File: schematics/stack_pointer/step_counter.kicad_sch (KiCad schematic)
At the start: 16 parts, among them U1 74HC00, U2 74HC193, U3 74HC193, U4 74HC193, U5 74HC193, U6 74HC245, U7 74HC245

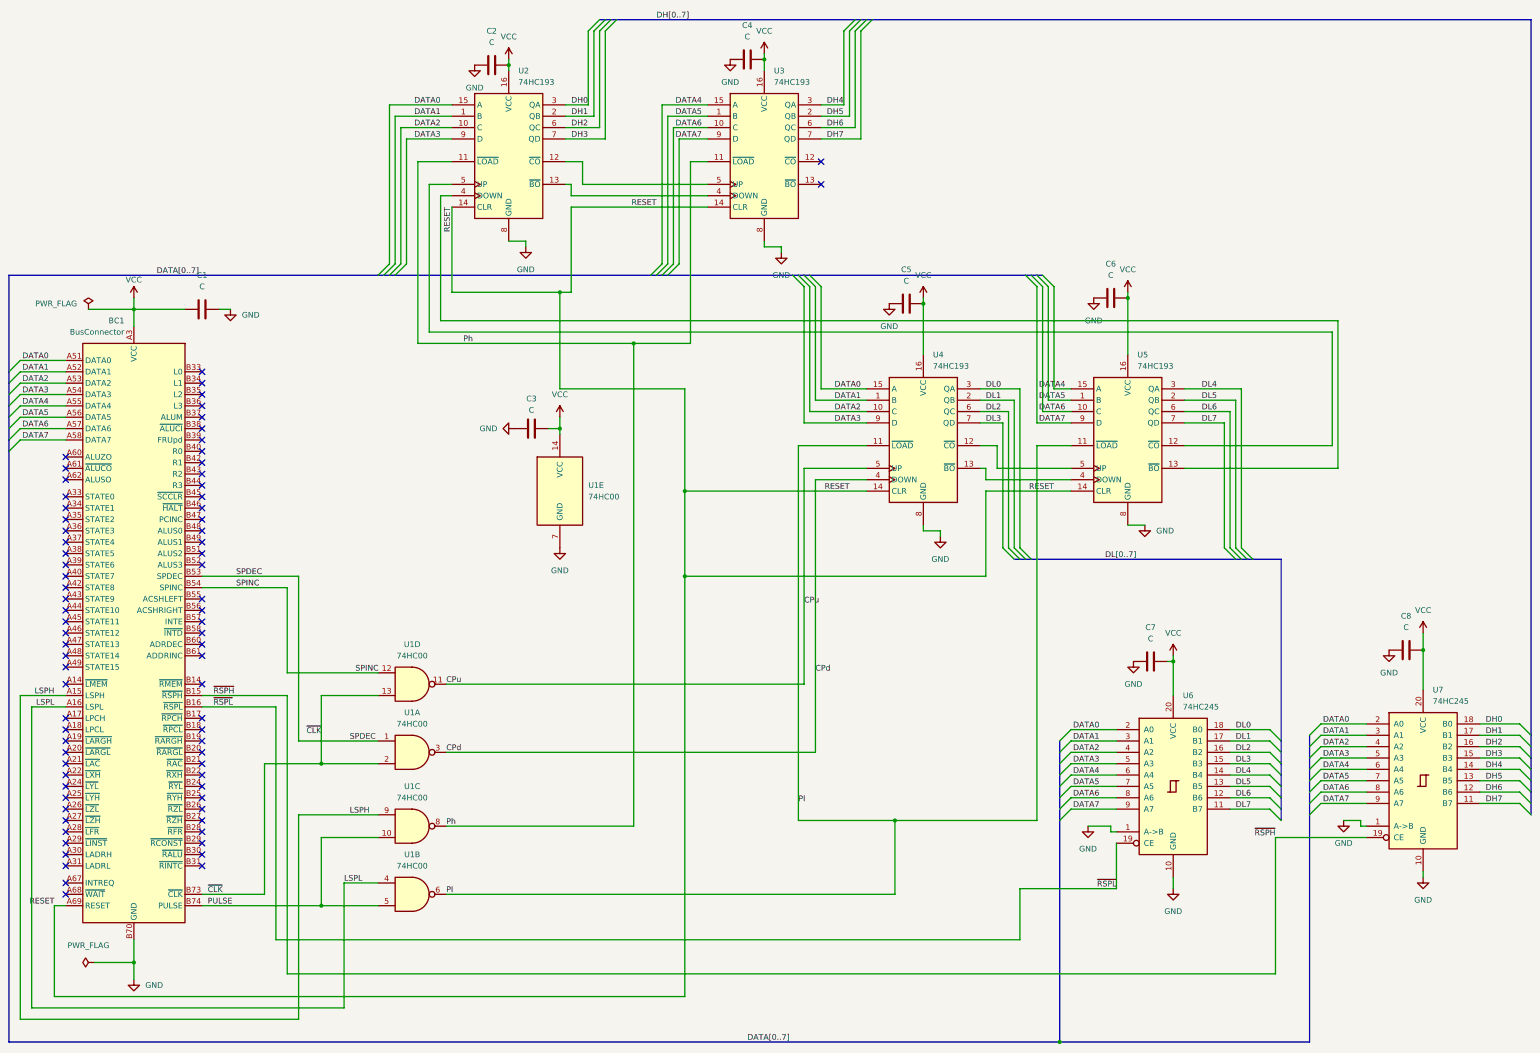
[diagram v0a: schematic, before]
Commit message: Add test points
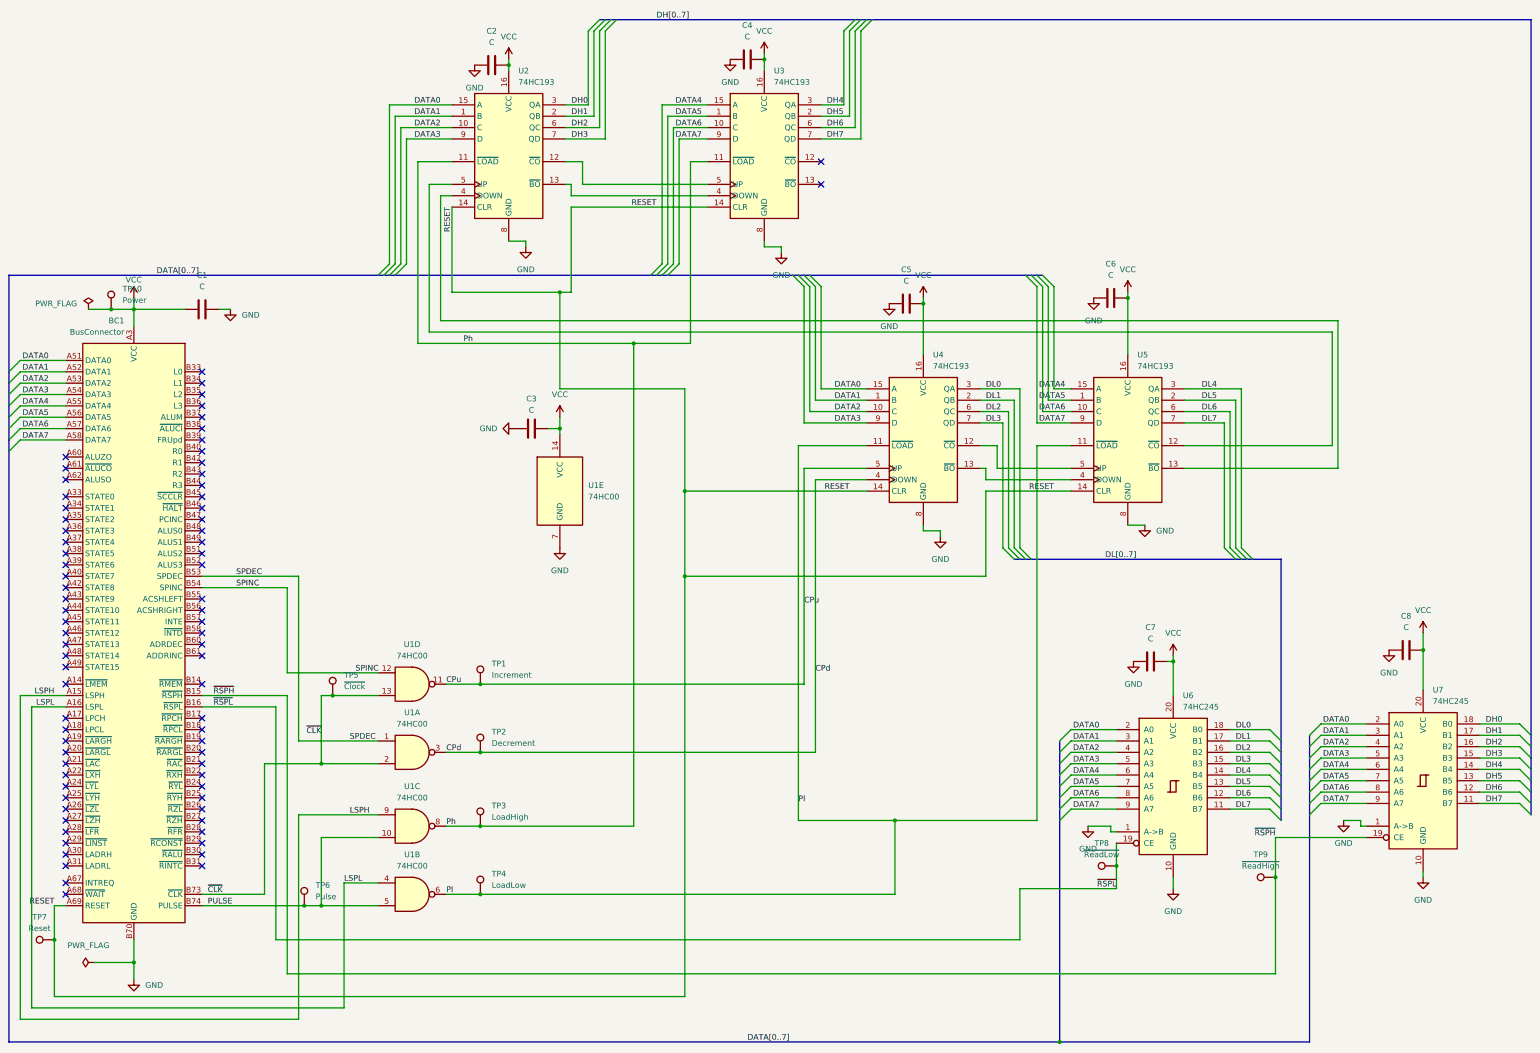
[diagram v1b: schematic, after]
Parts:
- added TP1: Increment, Connector_Pin:Pin_D1.0mm_L10.0mm, symbol Connector:TestPoint
- added TP10: Power, Connector_Pin:Pin_D1.0mm_L10.0mm, symbol Connector:TestPoint
- added TP2: Decrement, Connector_Pin:Pin_D1.0mm_L10.0mm, symbol Connector:TestPoint
- added TP3: LoadHigh, Connector_Pin:Pin_D1.0mm_L10.0mm, symbol Connector:TestPoint
- added TP4: LoadLow, Connector_Pin:Pin_D1.0mm_L10.0mm, symbol Connector:TestPoint
- added TP5: ~{Clock}, Connector_Pin:Pin_D1.0mm_L10.0mm, symbol Connector:TestPoint
- added TP6: Pulse, Connector_Pin:Pin_D1.0mm_L10.0mm, symbol Connector:TestPoint
- added TP7: Reset, Connector_Pin:Pin_D1.0mm_L10.0mm, symbol Connector:TestPoint
- added TP8: ~{ReadLow}, Connector_Pin:Pin_D1.0mm_L10.0mm, symbol Connector:TestPoint
- added TP9: ~{ReadHigh}, Connector_Pin:Pin_D1.0mm_L10.0mm, symbol Connector:TestPoint
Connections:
- net CPd: now also TP2.1
- net CPu: now also TP1.1
- net PULSE: now also TP6.1
- net Ph: now also TP3.1
- net Pl: now also TP4.1
- net RESET: now also TP7.1
- net VCC: now also TP10.1
- net ~{CLK}: now also TP5.1
- net ~{RSPH}: now also TP9.1
- net ~{RSPL}: now also TP8.1

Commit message: test points sp and pc
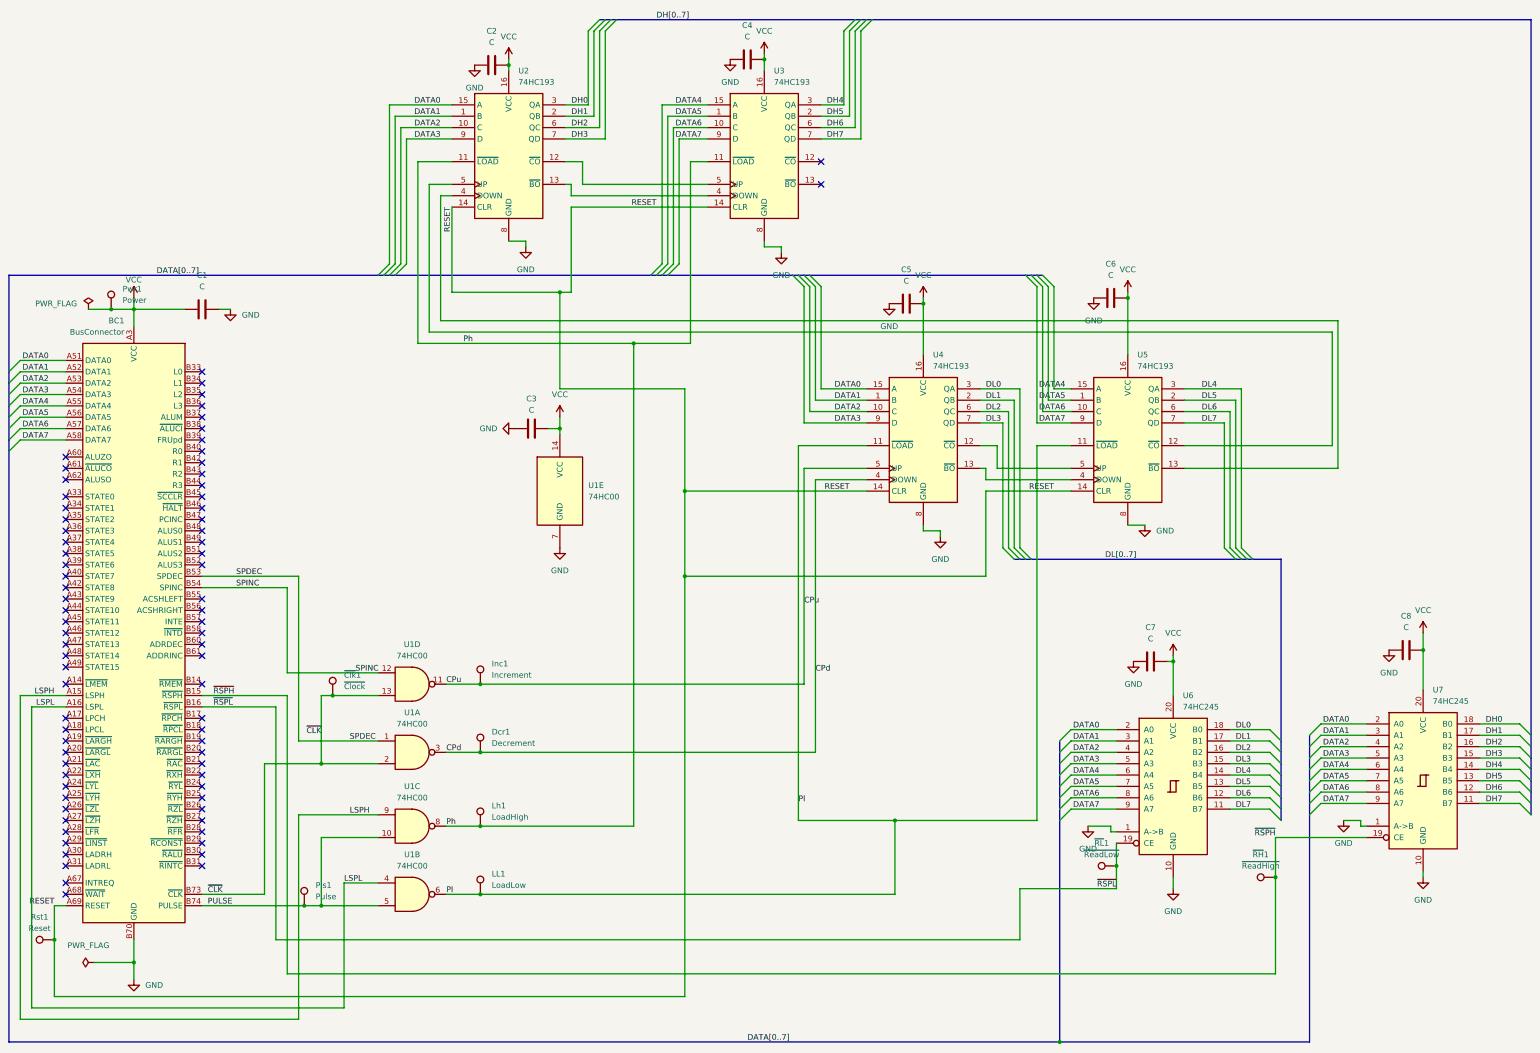
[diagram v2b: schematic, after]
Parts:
- Dcr1: renamed from TP2; footprint Connector_Pin:Pin_D1.0mm_L10.0mm -> TestPoint:TestPoint_Pad_D1.0mm
- Inc1: renamed from TP1; footprint Connector_Pin:Pin_D1.0mm_L10.0mm -> TestPoint:TestPoint_Pad_D1.0mm
- LL1: renamed from TP4; footprint Connector_Pin:Pin_D1.0mm_L10.0mm -> TestPoint:TestPoint_Pad_D1.0mm
- Lh1: renamed from TP3; footprint Connector_Pin:Pin_D1.0mm_L10.0mm -> TestPoint:TestPoint_Pad_D1.0mm
- Pls1: renamed from TP6; footprint Connector_Pin:Pin_D1.0mm_L10.0mm -> TestPoint:TestPoint_Pad_D1.0mm
- Pwr1: renamed from TP10; footprint Connector_Pin:Pin_D1.0mm_L10.0mm -> TestPoint:TestPoint_Pad_D1.0mm
- Rst1: renamed from TP7; footprint Connector_Pin:Pin_D1.0mm_L10.0mm -> TestPoint:TestPoint_Pad_D1.0mm
- ~{Clk}1: renamed from TP5; footprint Connector_Pin:Pin_D1.0mm_L10.0mm -> TestPoint:TestPoint_Pad_D1.0mm
- ~{RH}1: renamed from TP9; footprint Connector_Pin:Pin_D1.0mm_L10.0mm -> TestPoint:TestPoint_Pad_D1.0mm
- ~{RL}1: renamed from TP8; footprint Connector_Pin:Pin_D1.0mm_L10.0mm -> TestPoint:TestPoint_Pad_D1.0mm
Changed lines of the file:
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@@
 		(dnp no)
 		(fields_autoplaced yes)
-		(property "Reference" "TP6"
+		(property "Reference" "Pls1"
 			(at 101.6 215.1379 0)
 			(effects
@@
 			)
 		)
-		(property "Footprint" "Connector_Pin:Pin_D1.0mm_L10.0mm"
+		(property "Footprint" "TestPoint:TestPoint_Pad_D1.0mm"
 			(at 104.14 219.71 0)
 			(effects
@@
 			(project "step_counter"
 				(path "/f5389107-3d60-400a-ba2f-c69edfa4a2c5"
-					(reference "TP6")
+					(reference "Pls1")
 					(unit 1)
 				)
@@
 		(dnp no)
 		(fields_autoplaced yes)
-		(property "Reference" "TP3"
+		(property "Reference" "Lh1"
 			(at 140.97 197.3579 0)
 			(effects
@@
 			)
 		)
-		(property "Footprint" "Connector_Pin:Pin_D1.0mm_L10.0mm"
+		(property "Footprint" "TestPoint:TestPoint_Pad_D1.0mm"
 			(at 143.51 201.93 0)
 			(effects
@@
 			(project "step_counter"
 				(path "/f5389107-3d60-400a-ba2f-c69edfa4a2c5"
-					(reference "TP3")
+					(reference "Lh1")
 					(unit 1)
 				)
@@
 		(dnp no)
 		(fields_autoplaced yes)
-		(property "Reference" "TP1"
+		(property "Reference" "Inc1"
 			(at 140.97 165.6079 0)
 			(effects
@@
 			)
 		)
-		(property "Footprint" "Connector_Pin:Pin_D1.0mm_L10.0mm"
+		(property "Footprint" "TestPoint:TestPoint_Pad_D1.0mm"
 			(at 143.51 170.18 0)
 			(effects
@@
 			(project ""
 				(path "/f5389107-3d60-400a-ba2f-c69edfa4a2c5"
-					(reference "TP1")
+					(reference "Inc1")
 					(unit 1)
 				)
@@
 		(dnp no)
 		(fields_autoplaced yes)
-		(property "Reference" "TP5"
+		(property "Reference" "~{Clk}1"
 			(at 107.95 168.1479 0)
 			(effects
@@
 			)
 		)
-		(property "Footprint" "Connector_Pin:Pin_D1.0mm_L10.0mm"
+		(property "Footprint" "TestPoint:TestPoint_Pad_D1.0mm"
 			(at 110.49 172.72 0)
 			(effects
@@
 			(project "step_counter"
 				(path "/f5389107-3d60-400a-ba2f-c69edfa4a2c5"
-					(reference "TP5")
+					(reference "~{Clk}1")
 					(unit 1)
 				)
@@
 		(dnp no)
 		(fields_autoplaced yes)
-		(property "Reference" "TP10"
+		(property "Reference" "Pwr1"
 			(at 58.42 81.7879 0)
 			(effects
@@
 			)
 		)
-		(property "Footprint" "Connector_Pin:Pin_D1.0mm_L10.0mm"
+		(property "Footprint" "TestPoint:TestPoint_Pad_D1.0mm"
 			(at 60.96 86.36 0)
 			(effects
@@
 			(project "step_counter"
 				(path "/f5389107-3d60-400a-ba2f-c69edfa4a2c5"
-					(reference "TP10")
+					(reference "Pwr1")
 					(unit 1)
 				)
@@
 		(dnp no)
 		(fields_autoplaced yes)
-		(property "Reference" "TP9"
+		(property "Reference" "~{RH}1"
 			(at 312.928 208.28 90)
 			(effects
@@
 			)
 		)
-		(property "Footprint" "Connector_Pin:Pin_D1.0mm_L10.0mm"
+		(property "Footprint" "TestPoint:TestPoint_Pad_D1.0mm"
 			(at 316.23 208.28 0)
 			(effects
@@
 			(project "step_counter"
 				(path "/f5389107-3d60-400a-ba2f-c69edfa4a2c5"
-					(reference "TP9")
+					(reference "~{RH}1")
 					(unit 1)
 				)
@@
 		(dnp no)
 		(fields_autoplaced yes)
-		(property "Reference" "TP4"
+		(property "Reference" "LL1"
 			(at 140.97 212.5979 0)
 			(effects
@@
 			)
 		)
-		(property "Footprint" "Connector_Pin:Pin_D1.0mm_L10.0mm"
+		(property "Footprint" "TestPoint:TestPoint_Pad_D1.0mm"
 			(at 143.51 217.17 0)
 			(effects
@@
 			(project "step_counter"
 				(path "/f5389107-3d60-400a-ba2f-c69edfa4a2c5"
-					(reference "TP4")
+					(reference "LL1")
 					(unit 1)
 				)
@@
 		(dnp no)
 		(fields_autoplaced yes)
-		(property "Reference" "TP8"
+		(property "Reference" "~{RL}1"
 			(at 277.368 205.74 90)
 			(effects
@@
 			)
 		)
-		(property "Footprint" "Connector_Pin:Pin_D1.0mm_L10.0mm"
+		(property "Footprint" "TestPoint:TestPoint_Pad_D1.0mm"
 			(at 280.67 205.74 0)
 			(effects
@@
 			(project "step_counter"
 				(path "/f5389107-3d60-400a-ba2f-c69edfa4a2c5"
-					(reference "TP8")
+					(reference "~{RL}1")
 					(unit 1)
 				)
@@
 		(dnp no)
 		(fields_autoplaced yes)
-		(property "Reference" "TP2"
+		(property "Reference" "Dcr1"
 			(at 140.97 180.8479 0)
 			(effects
@@
 			)
 		)
-		(property "Footprint" "Connector_Pin:Pin_D1.0mm_L10.0mm"
+		(property "Footprint" "TestPoint:TestPoint_Pad_D1.0mm"
 			(at 143.51 185.42 0)
 			(effects
@@
 			(project "step_counter"
 				(path "/f5389107-3d60-400a-ba2f-c69edfa4a2c5"
-					(reference "TP2")
+					(reference "Dcr1")
 					(unit 1)
 				)
@@
 		(dnp no)
 		(fields_autoplaced yes)
-		(property "Reference" "TP7"
+		(property "Reference" "Rst1"
 			(at 39.878 222.25 90)
 			(effects
@@
 			)
 		)
-		(property "Footprint" "Connector_Pin:Pin_D1.0mm_L10.0mm"
+		(property "Footprint" "TestPoint:TestPoint_Pad_D1.0mm"
 			(at 43.18 222.25 0)
 			(effects
@@
 			(project "step_counter"
 				(path "/f5389107-3d60-400a-ba2f-c69edfa4a2c5"
-					(reference "TP7")
+					(reference "Rst1")
 					(unit 1)
 				)
